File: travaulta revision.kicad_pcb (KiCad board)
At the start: 4 copper layers, 209.7 x 76.4 mm, 106 parts, among them SW1 EC_SW, SW10 EC_SW, SW11 EC_SW, SW12 EC_SW, SW13 EC_SW, SW14 EC_SW, SW15 EC_SW, SW16 EC_SW, SW17 EC_SW, SW18 EC_SW, SW19 EC_SW, SW2 EC_SW, SW20 EC_SW, SW21 EC_SW, SW22 EC_SW, SW23 EC_SW, SW24 EC_SW, SW25 EC_SW, SW26 EC_SW, SW27 EC_SW, SW28 EC_SW, SW29 EC_SW, SW3 EC_SW, SW30 EC_SW, SW31 EC_SW, SW32 EC_SW, SW33 EC_SW, SW34 EC_SW, SW35 EC_SW, SW36 EC_SW, SW37 EC_SW, SW38 BOOT0, SW4 EC_SW, SW5 EC_SW, SW6 EC_SW, SW7 EC_SW, SW8 EC_SW, SW9 EC_SW, U1 STM32F401CBUx, U2 XC6206PxxxMR, U3 74HC4051, U4 74HC4051, U5 OPA350, Y1 8 MHz

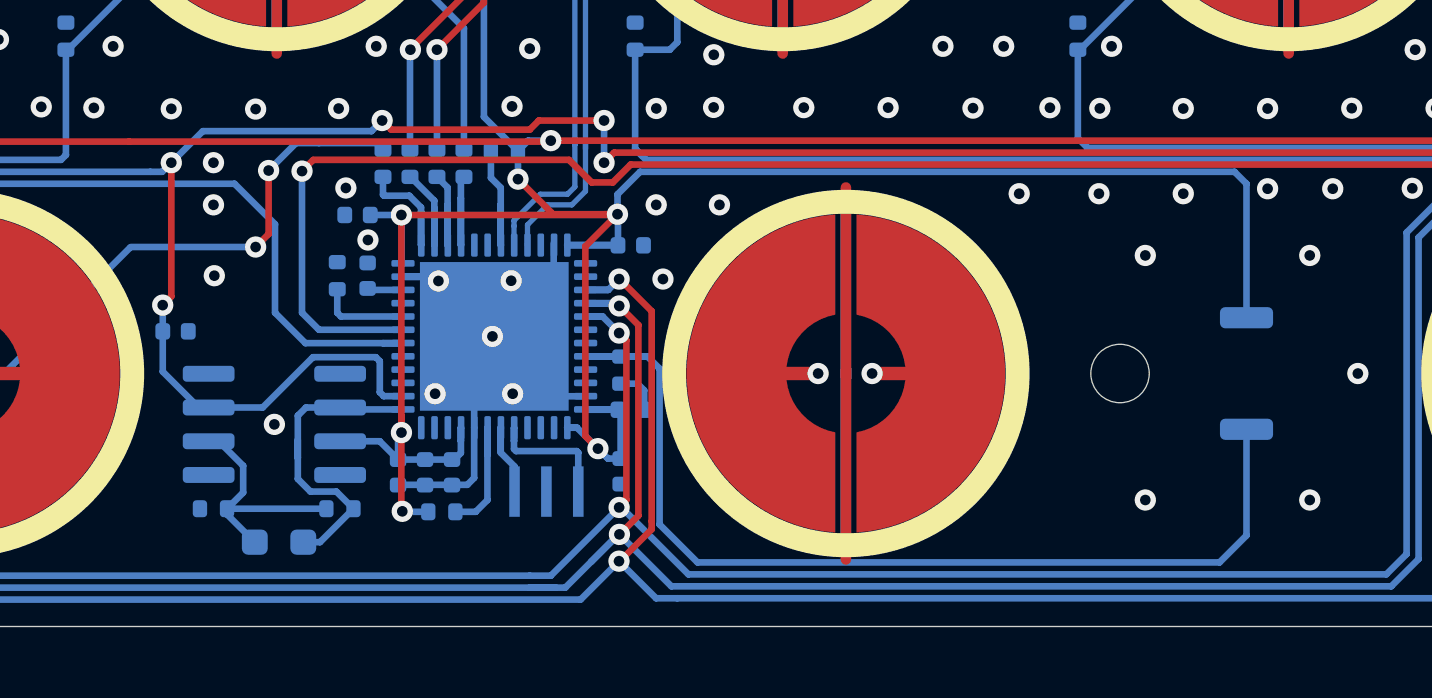
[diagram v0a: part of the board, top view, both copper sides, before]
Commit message: reset button simplified
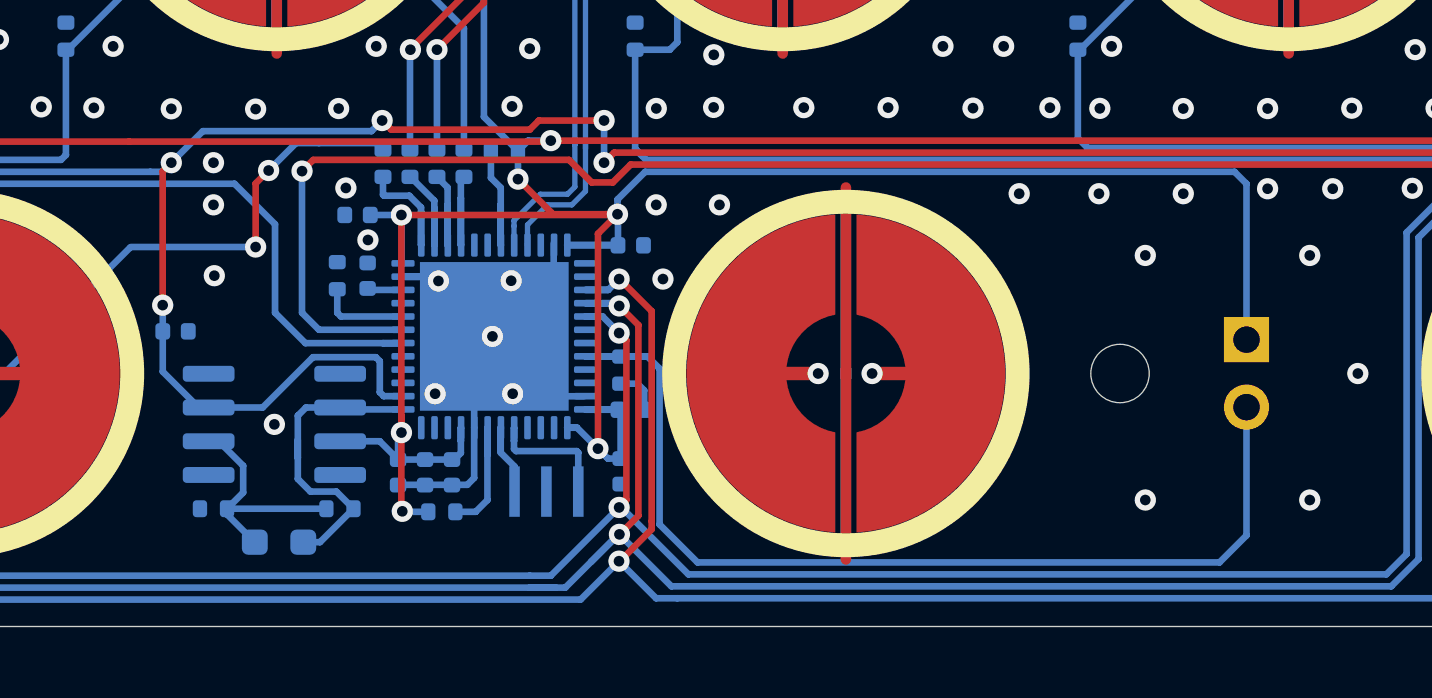
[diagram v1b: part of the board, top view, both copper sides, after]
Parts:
- SW38: footprint Button_Switch_SMD:SW_Push_SPST_NO_Alps_SKRK -> Connector_PinHeader_2.54mm:PinHeader_1x02_P2.54mm_Vertical
- moved SW38 1.27 mm to (181.0, 113.0), turned to 180 degrees
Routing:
- net BOOT0: track 38.3 -> 39.1 mm
